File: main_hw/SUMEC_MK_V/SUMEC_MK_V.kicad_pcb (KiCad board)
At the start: 4 copper layers, 97 x 37.5 mm, 116 parts, among them IC1 TPS565242DRLR, IC2 DRV8874PWPR, IC3 DRV8874PWPR, J1 XT30PW-M, J10 Conn_01x03_Pin, J11 Conn_01x03_Pin, J12 Conn_01x03_Pin, J13 Conn_01x03_Pin, J14 Conn_01x03_Pin, J15 Conn_01x03_Pin, J2 Conn_01x06_Socket, J3 Conn_01x06_Socket, J4 USB_TypeC, J5 Conn_01x04_Pin, J6 Conn_01x06_Pin, J7 Conn_01x06_Pin, J8 Conn_01x03_Pin, J9 Conn_01x06_Pin, Q1 Q_PMOS, Q2 Q_PMOS, SW1 SW_DPDT_x2, SW2 SW_Push, SW3 SW_Push, SW4 SW_Push, SW5 SW_Push, U1 INA226, U2 TPS62133, U3 AP62301Z6, U4 24CW1280T-I/OT, U5 ESP32-S3-WROOM-1, U6 USBLC6-2SC6, U7 BMI088

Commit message: PCB update - layout
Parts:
- R28: moved to B.Cu
- moved C32 52.2 mm to (157.4, 60.0), turned to -90 degrees
- moved U7 51.1 mm to (154.7, 60.0), turned to -90 degrees
- moved C34 50.3 mm to (151.9, 60.0), turned to -90 degrees
- moved C24 46.1 mm to (158.2, 65.6), turned to 90 degrees
- moved U4 44.5 mm to (155.1, 65.7), turned to 0 degrees
- moved R27 37.0 mm to (167.7, 66.2), turned to 0 degrees
- moved R17 28.0 mm to (137.8, 63.6), turned to 0 degrees
- moved TP8 27.1 mm to (176.0, 59.5)
- moved TP7 25.5 mm to (153.2, 70.8)
- moved JP3 22.6 mm to (142.7, 55.1), turned to 180 degrees
- moved R18 19.3 mm to (139.9, 59.2), turned to 180 degrees
- moved IC3 17.6 mm to (142.0, 59.2), turned to 0 degrees
- moved C18 17.4 mm to (146.9, 57.9), turned to -90 degrees
- moved D3 17.3 mm to (160.0, 71.3)
- moved R19 17.2 mm to (139.9, 61.1), turned to 180 degrees
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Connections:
- J13 pad 1: GND -> IR_MODULE
- J13 pad 2: IR_MODULE -> unconnected-(J13-Pin_2-Pad2)
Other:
- board text added: "3V3 CONV"
- board text added: "5V CONV OLD"
- board text added: "BUZZER (BACK)"
- board text added: "EEPROM"
- board text added: "IMU"
- board text added: "IR MODULE"
- board text added: "LEDS"
- board text added: "MOSFER SWITCH"
- board text added: "MOT. DRIVERS"
- board text added: "USB VBUS SWITCH"
- board text added: "VOLT. READER (BACK)"
- board text removed: "- DEAL WITH THIS"

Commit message: pcb routing
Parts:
- moved TP7 11.7 mm to (161.9, 63.0)
- moved Q2 9.95 mm to (163.6, 68.0)
- moved R6 9.95 mm to (165.7, 70.3)
- moved C24 4.18 mm to (155.1, 68.4), turned to 180 degrees
- moved R28 2.07 mm to (157.9, 71.8)
- moved D3 2.06 mm to (157.9, 71.5)
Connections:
- net Net-(Q2-G) renamed /POWER_SUPPLY/FET_SW
- J13 pad 2: unconnected-(J13-Pin_2-Pad2) -> GND
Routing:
- net +3V3: track 9.54 -> 21.5 mm, vias 2 -> 3
- net +3.3V: track 0.00 -> 11.6 mm
- net GND: track 7.02 -> 13.7 mm
- net VBATT_SHUNT: track 12.1 -> 7.31 mm, vias 2 -> 3
- net PMODE_2: track 0.00 -> 3.56 mm
- net Net-(IC3-CPL): track 0.00 -> 3.00 mm
- net /POWER_SUPPLY/FET_SW: track 1.69 -> 0.00 mm, vias 0 -> 2
- net EN: track 0.00 -> 1.04 mm, vias 0 -> 2
- net BOOT: track 0.00 -> 0.66 mm, vias 0 -> 1
- added copper zone on F.Cu, net +12V
- added copper zone on B.Cu, net /POWER_SUPPLY/FET_SW
- added copper zone on F.Cu, net /POWER_SUPPLY/FET_SW
- added copper zone on B.Cu, net GND
- added copper zone on F.Cu, net VBATT_SHUNT
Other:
- board text added: "EEPROwoM"
- board text removed: "EEPROM"

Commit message: routing update
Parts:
- R34, R35: moved to B.Cu
- moved R35 8.91 mm to (130.8, 60.8), turned to 90 degrees
- moved R34 6.52 mm to (125.8, 58.0), turned to 0 degrees
- moved C13 0.30 mm to (127.2, 63.4)
- moved R11 0.25 mm to (127.2, 59.4)
- moved R12 0.25 mm to (127.2, 61.4)
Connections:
- net Net-(U3-FB) renamed /POWER_SUPPLY/FB_5V
- net Net-(U3-SW) renamed /POWER_SUPPLY/SW
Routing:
- net VOUT_5V: track 0.00 -> 79.6 mm, vias 0 -> 1
- net VBUS_USB: track 0.48 -> 16.3 mm, vias 0 -> 1
- net Net-(F1-Pad2): track 0.00 -> 7.39 mm
- net Net-(U3-EN): track 0.00 -> 7.18 mm, vias 0 -> 2
- net +5V: track 0.00 -> 6.00 mm, vias 0 -> 2
- net D_NEG_IN: track 0.00 -> 4.81 mm
- net D_POS_IN: track 0.00 -> 3.74 mm
- net FB: track 0.00 -> 3.41 mm
- net QRE_BACK: track 0.00 -> 2.94 mm
- net Net-(J8-Pin_2): track 0.00 -> 2.20 mm
- net +3V3: track 21.5 -> 23.6 mm
- net /CONNECTIVITY/SHLD: track 0.00 -> 2.02 mm
- net /POWER_SUPPLY/FB_5V: track 0.00 -> 1.75 mm
- net Net-(D1-A): track 0.00 -> 1.69 mm, vias 0 -> 1
- net Net-(U3-BST): track 0.00 -> 1.58 mm
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- added copper zone on F.Cu, net +3V3
- added copper zone on F.Cu, net +5V
- added copper zone on F.Cu, net /POWER_SUPPLY/SW
- added copper zone on F.Cu, net FB
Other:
- board text added: "0"
- board text added: "0 mm"
- board text added: "0.01 mm"
- board text added: "0.02"
- board text added: "0.035 mm"
- board text added: "0.1 mm"
- board text added: "1"
- board text added: "1.24 mm"
- board text added: "3.3"
- board text added: "4.5"
- board text added: "B.Paste"
- board text added: "B.Silkscreen"
- board text added: "B.SolderMask"
- board text added: "Back.Cu"
- board text added: "Bottom Silk Screen"
- board text added: "Bottom Solder Mask"
- board text added: "Bottom Solder Paste"
- board text added: "Color"
- board text added: "Dielectric"
- board text added: "Epsilon R"
- board text added: "F.Paste"
- board text added: "F.Silkscreen"
- board text added: "F.SolderMask"
- board text added: "FR4"
- board text added: "FR4 natural"
- board text added: "Front.Cu"
- board text added: "In1.Cu"
- board text added: "In2.Cu"
- board text added: "Layer Name"
- board text added: "Loss Tangent"
- board text added: "Material"
- board text added: "Not specified"
- board text added: "Thickness (mm)"
- board text added: "Top Silk Screen"
- board text added: "Top Solder Mask"
- board text added: "Top Solder Paste"
- board text added: "Type"
- board text added: "copper"
- board text added: "core"
- board text added: "prepreg"

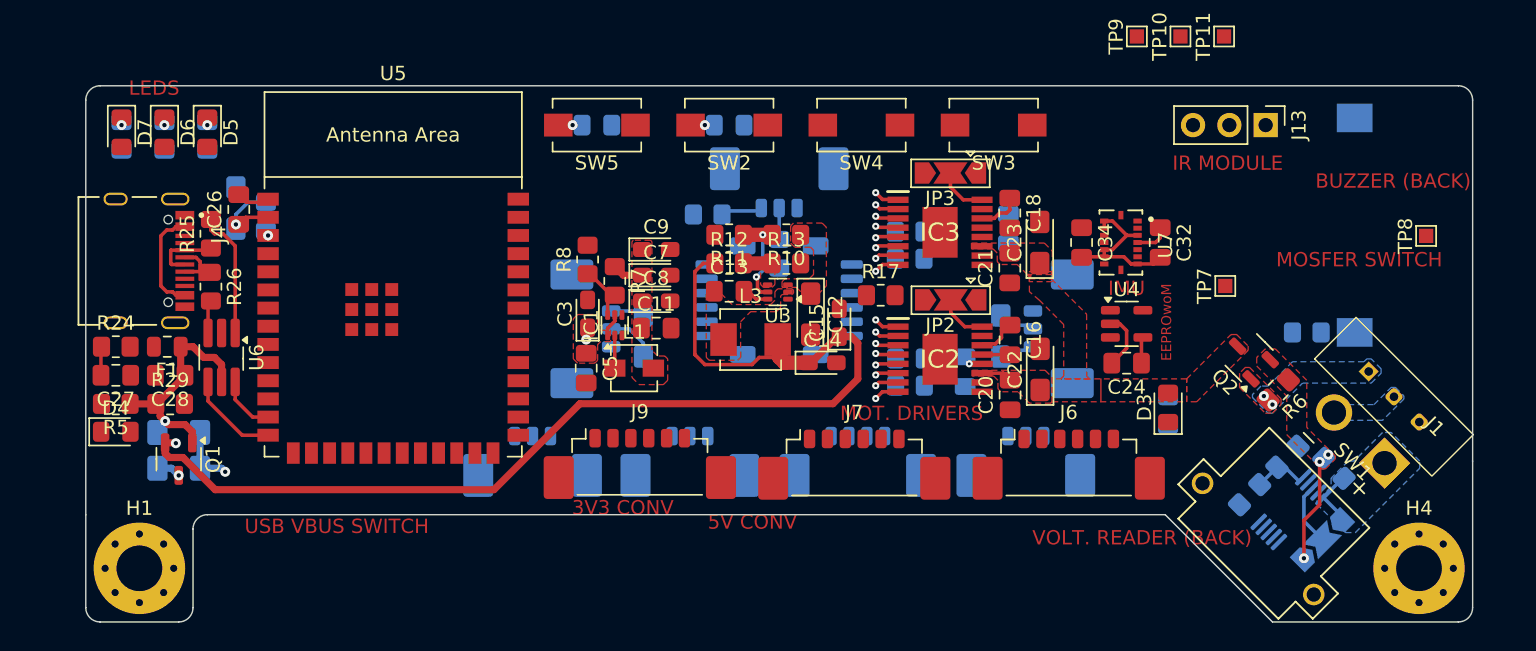
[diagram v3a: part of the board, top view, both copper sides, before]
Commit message: PCB pours update
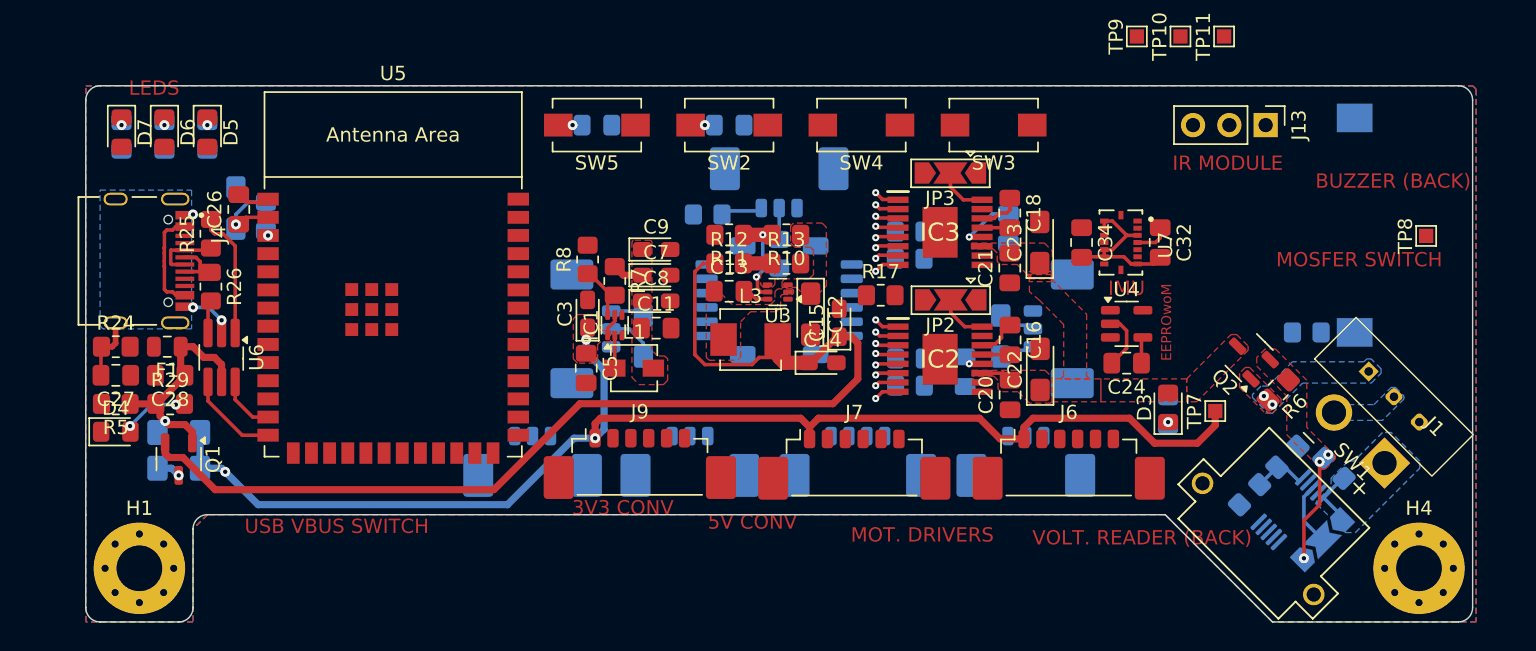
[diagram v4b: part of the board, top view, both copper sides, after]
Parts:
- moved TP7 8.78 mm to (161.2, 71.8)
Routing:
- net +5V: track 6.00 -> 92.3 mm, vias 2 -> 3
- net Net-(D4-A): track 0.00 -> 4.85 mm, vias 0 -> 2
- net GND: track 13.7 -> 17.6 mm, vias 0 -> 3
- net Net-(IC3-VCP): track 0.00 -> 3.45 mm, vias 0 -> 1
- net /CONNECTIVITY/SHLD: track 2.02 -> 4.54 mm
- net Net-(IC3-CPH): track 0.00 -> 1.94 mm
- net VOUT_5V: track 79.6 -> 78.8 mm, vias 1 -> 0
- net Net-(D3-K): vias 0 -> 1
- added copper zone on B.Cu, net /CONNECTIVITY/SHLD
- added copper zone on F.Cu, net GND

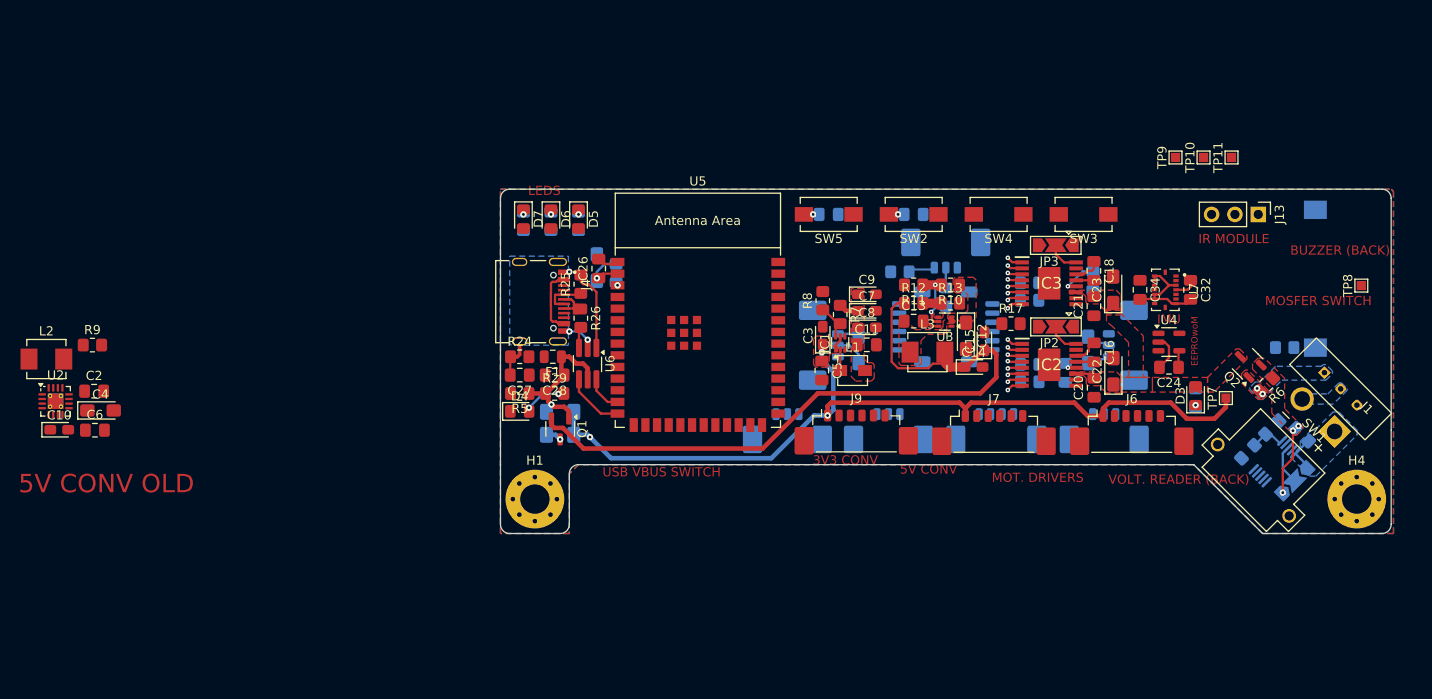
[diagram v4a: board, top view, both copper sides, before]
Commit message: PCB Update, signal routing
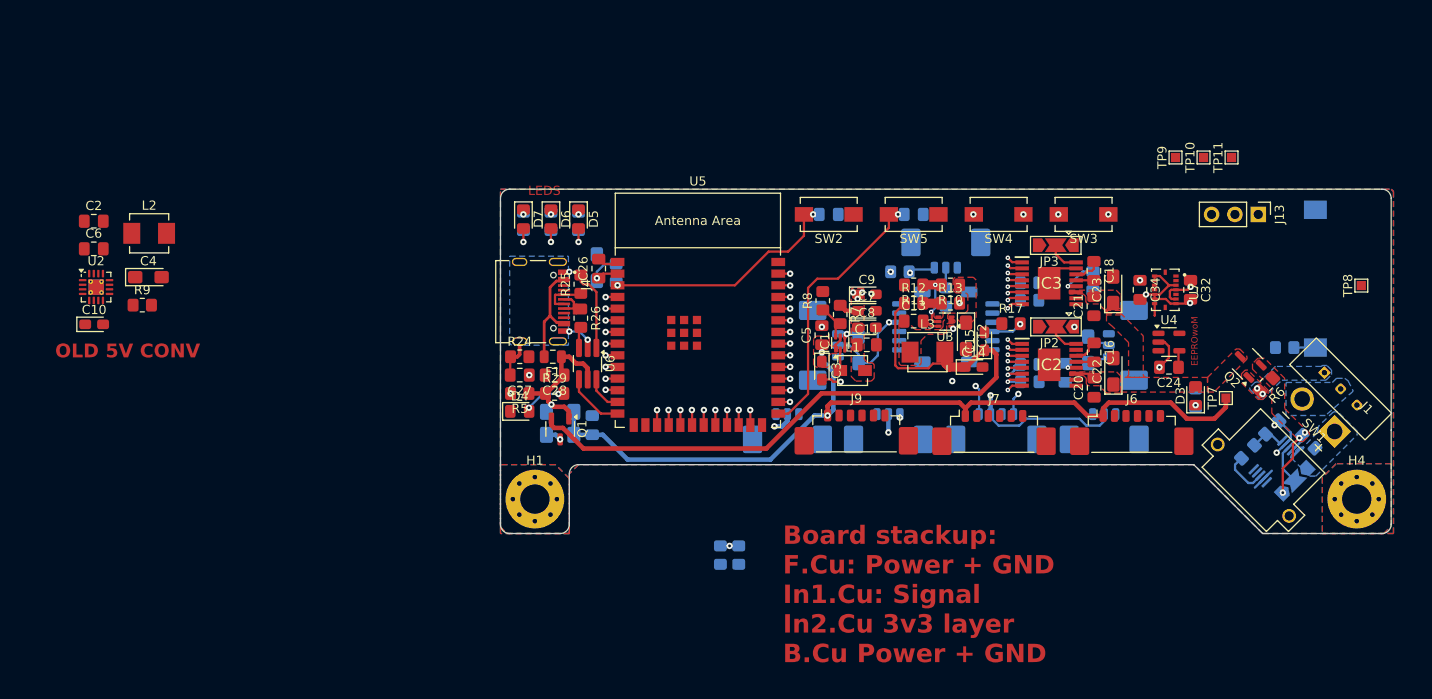
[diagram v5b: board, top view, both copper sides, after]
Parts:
- added C35: 100nF, Capacitor_SMD:C_0805_2012Metric_Pad1.18x1.45mm_HandSolder, B.Cu at (92.2, 74.7)
- added R36: 10k, Resistor_SMD:R_0805_2012Metric_Pad1.20x1.40mm_HandSolder, B.Cu at (108.2, 88.8)
- added R37: 10k, Resistor_SMD:R_0805_2012Metric_Pad1.20x1.40mm_HandSolder, B.Cu at (106.2, 88.8)
- moved C6 19.8 mm to (38.0, 55.5)
- moved C2 18.5 mm to (38.0, 52.5)
- moved L2 17.7 mm to (44.0, 53.8)
- moved C4 15.4 mm to (43.9, 58.6)
- moved U2 13.2 mm to (38.2, 59.7)
- moved C10 12.1 mm to (38.0, 63.7)
- moved C29 9.25 mm to (118.0, 51.8)
- moved C30 9.25 mm to (127.2, 51.8)
- moved SW2 9.25 mm to (118.0, 51.8)
- moved SW5 9.25 mm to (127.2, 51.8)
- moved R9 6.96 mm to (43.2, 61.6)
- moved C5 3.85 mm to (117.2, 64.9), turned to 90 degrees
- moved C3 3.80 mm to (117.2, 68.8), turned to -90 degrees
- moved R4 1.03 mm to (170.2, 76.5)
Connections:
- C32 pad 2: +3.3V -> +3V3
- C34 pad 2: +3.3V -> +3V3
- U7 pad 10: +3.3V -> +3V3
- U7 pad 11: +3.3V -> +3V3
- U7 pad 14: +3.3V -> +3V3
- U7 pad 15: +3.3V -> +3V3
- U7 pad 3: +3.3V -> +3V3
- U7 pad 7: +3.3V -> +3V3
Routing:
- net IR_MODULE: track 0.00 -> 53.5 mm
- net +3V3: track 23.6 -> 69.3 mm, vias 3 -> 18
- net BOOT: track 0.66 -> 29.3 mm
- net nSLEEP: track 3.23 -> 28.5 mm
- net nFAULT: track 3.19 -> 28.3 mm
- net PH_L: track 1.68 -> 26.6 mm
- net EN: track 1.04 -> 25.9 mm
- net EN_L: track 1.76 -> 26.2 mm
- net EN_R: track 1.76 -> 25.0 mm
- net PH_R: track 1.68 -> 24.8 mm
- net GND: track 17.6 -> 36.1 mm, vias 3 -> 17
- net QRE_BACK: track 2.94 -> 16.7 mm, vias 0 -> 1
- net +3.3V: track 11.6 -> 0.00 mm
- net LED_3: track 0.00 -> 11.4 mm, vias 0 -> 1
- net LED_2: track 0.00 -> 8.75 mm, vias 0 -> 1
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- added copper zone on In2.Cu, net +3V3
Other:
- board text added: "0,0900 mm / 0,0900 mm"
- board text added: "0,1000 mm"
- board text added: "1,6000 mm"
- board text added: "4"
- board text added: "97,0000 mm x 37,5000 mm"
- board text added: "BOARD CHARACTERISTICS"
- board text added: "Board Thickness:"
- board text added: "Board overall dimensions:"
- board text added: "Board stackup: F.Cu: Power + GND In1.Cu: Signal In2.Cu 3v3 layer B.Cu Power + GND"
- board text added: "Castellated pads:"
- board text added: "Copper Finish:"
- board text added: "Copper Layer Count:"
- board text added: "Edge card connectors:"
- board text added: "HAL lead-free"
- board text added: "Impedance Control:"
- board text added: "Min hole diameter:"
- board text added: "Min track/spacing:"
- board text added: "No"
- board text added: "OLD 5V CONV"
- board text added: "Plated Board Edge:"
- board text removed: "0"
- board text removed: "0 mm"
- board text removed: "0.01 mm"
- board text removed: "0.02"
- board text removed: "0.035 mm"
- board text removed: "0.1 mm"
- board text removed: "1"
- board text removed: "1.24 mm"
- board text removed: "3.3"
- board text removed: "3V3 CONV"
- board text removed: "4.5"
- board text removed: "5V CONV"
- board text removed: "5V CONV OLD"
- board text removed: "B.Paste"
- board text removed: "B.Silkscreen"
- board text removed: "B.SolderMask"
- board text removed: "BUZZER (BACK)"
- board text removed: "Back.Cu"
- board text removed: "Bottom Silk Screen"
- board text removed: "Bottom Solder Mask"
- board text removed: "Bottom Solder Paste"
- board text removed: "Color"
- board text removed: "Dielectric"
- board text removed: "Epsilon R"
- board text removed: "F.Paste"
- board text removed: "F.Silkscreen"
- board text removed: "F.SolderMask"
- board text removed: "FR4"
- board text removed: "FR4 natural"
- board text removed: "Front.Cu"
- board text removed: "IMU"
- board text removed: "IR MODULE"
- board text removed: "In1.Cu"
- board text removed: "In2.Cu"
- board text removed: "Layer Name"
- board text removed: "Loss Tangent"
- board text removed: "MOSFER SWITCH"
- board text removed: "MOT. DRIVERS"
- board text removed: "Material"
- board text removed: "Not specified"
- board text removed: "Thickness (mm)"
- board text removed: "Top Silk Screen"
- board text removed: "Top Solder Mask"
- board text removed: "Top Solder Paste"
- board text removed: "Type"
- board text removed: "USB VBUS SWITCH"
- board text removed: "VOLT. READER (BACK)"
- board text removed: "copper"
- board text removed: "core"
- board text removed: "prepreg"
